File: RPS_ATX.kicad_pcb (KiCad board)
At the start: 2 copper layers, 100 x 50 mm, 89 parts, among them J1 5V, J2 C1, J3 C2, J4 17.5V, J5 PS_OUT-, J6 PS_OUT+, J7 RPS_OUT+, J8 Conn_01x05, J9 RPS_OUT-, Q1 AO3400A, Q3 BSS138, SW1 RST, U1 TL494, U2 AMS1117-3.3, U3 L7815, U4 NE5532, U5 INA180A2, U6 ICL7660, U7 LM7805_TO220, U8 STM32G431RBT6, Y1 8MHz

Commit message: approximate location of the components at the PCB
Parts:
- removed SW1: RST, Button_Switch_SMD:SW_Push_1P1T_NO_E-Switch_TL3301NxxxxxG
- added SW2: RST, Button_Switch_SMD:SW_Push_1P1T_NO_E-Switch_TL3301NxxxxxG, F.Cu at (132.3, 93.8)
- J8: value Conn_01x05 -> SWD
- moved Q1 209.6 mm to (66.9, 93.0), turned to 180 degrees
- moved C17 201.9 mm to (79.5, 97.0), turned to 180 degrees
- moved C13 200.8 mm to (84.5, 99.6)
- moved C14 192.2 mm to (90.5, 94.9), turned to -90 degrees
- moved FB2 190.0 mm to (104.9, 87.9), turned to -90 degrees
- moved J3 186.9 mm to (88.1, 57.5)
- moved R12 185.6 mm to (61.8, 93.0), turned to 180 degrees
- moved J2 184.8 mm to (91.9, 57.5)
- moved TP1 184.6 mm to (91.2, 99.2), turned to 90 degrees
- moved C3 176.0 mm to (82.6, 71.3), turned to 180 degrees
- moved R10 175.9 mm to (105.0, 82.7), turned to 90 degrees
- moved C19 175.0 mm to (83.6, 65.8), turned to 90 degrees
- moved R19 174.5 mm to (119.4, 71.6), turned to 90 degrees
- moved C28 174.1 mm to (107.4, 87.8), turned to -90 degrees
- moved C30 171.9 mm to (107.4, 82.7), turned to 90 degrees
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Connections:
- net MEAS_U+ renamed VOUT
- C1 pad 2: MEAS_I- -> GND
- C10 pad 2: MEAS_I- -> GND
- C11 pad 2: MEAS_I- -> GND
- C12 pad 2: MEAS_I- -> GND
- C13 pad 2: MEAS_I- -> GND
- C14 pad 2: MEAS_I- -> GND
- C16 pad 2: MEAS_I- -> GND
- C17 pad 1: +17.5V_ATX -> GND
- C17 pad 2: MEAS_I- -> +5V
- C18 pad 2: MEAS_I- -> GND
- C19 pad 2: MEAS_I- -> GND
- C2 pad 2: MEAS_I- -> GND
- C21 pad 2: MEAS_I- -> GND
- C22 pad 2: MEAS_I- -> GND
- C23 pad 2: MEAS_I- -> GND
- C24 pad 2: MEAS_I- -> GND
- C25 pad 2: MEAS_I- -> GND
- C26 pad 2: MEAS_I- -> GND
- C27 pad 2: MEAS_I- -> GND
- C28 pad 2: MEAS_I- -> GND
- C29 pad 2: MEAS_I- -> GND
- C3 pad 2: MEAS_I- -> GND
- C30 pad 2: MEAS_I- -> GND
- C31 pad 2: MEAS_I- -> GND
- C32 pad 2: MEAS_I- -> GND
- C33 pad 2: MEAS_I- -> GND
- C4 pad 1: MEAS_I- -> GND
- C5 pad 2: MEAS_I- -> GND
- C6 pad 2: MEAS_I- -> GND
- C7 pad 2: MEAS_I- -> GND
- C8 pad 2: MEAS_I- -> GND
- C9 pad 2: MEAS_I- -> GND
- J5 pad 1: MEAS_I- -> GND
- J8 pad 1: MCU_SWDIO -> MCU_RST
- J8 pad 2: MCU_SWCLK -> MCU_SWDIO
- J8 pad 3: MCU_SWO -> MCU_SWCLK
- J8 pad 4: MCU_RST -> MCU_SWO
- J8 pad 5: MEAS_I- -> GND
- Q3 pad 2: MEAS_I- -> GND
- R11 pad 1: MEAS_I- -> GND
- R18 pad 1: MEAS_I- -> GND
- R23 pad 2: MEAS_I- -> GND
- R3 pad 1: MEAS_I- -> GND
- R8 pad 2: MEAS_I- -> GND
- R9 pad 2: MEAS_I- -> GND
- U1 pad 10: MEAS_I- -> GND
- U1 pad 7: MEAS_I- -> GND
- U1 pad 9: MEAS_I- -> GND
- U2 pad 1: MEAS_I- -> GND
- U3 pad 2: MEAS_I- -> GND
- U4 pad 5: MEAS_I- -> GND
- U5 pad 2: MEAS_I- -> GND
- U6 pad 3: MEAS_I- -> GND
- U7 pad 2: MEAS_I- -> GND
- U8 pad 15: MEAS_I- -> GND
- U8 pad 27: MEAS_I- -> GND
- U8 pad 31: MEAS_I- -> GND
- U8 pad 47: MEAS_I- -> GND
- U8 pad 63: MEAS_I- -> GND

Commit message: final location of the power,analog sections
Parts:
- removed SW2: RST, Button_Switch_SMD:SW_Push_1P1T_NO_E-Switch_TL3301NxxxxxG
- added JP1: RST, TestPoint:TestPoint_2Pads_Pitch2.54mm_Drill0.8mm, F.Cu at (127.0, 100.3)
- added L1: L, my lib:Resistor_Shunt_L10_D3.7, F.Cu at (59.8, 63.2)
- added R20: 5.1K, Resistor_SMD:R_1206_3216Metric_Pad1.30x1.75mm_HandSolder, F.Cu at (121.0, 100.3)
- Y1: footprint Crystal:Crystal_SMD_MicroCrystal_CC1V-T1A-2Pin_8.0x3.7mm_HandSoldering -> Crystal:Crystal_SMD_0603-2Pin_6.0x3.5mm_HandSoldering
- moved C10 63.4 mm to (172.1, 122.6)
- moved C6 63.4 mm to (172.1, 115.1)
- moved J1 63.4 mm to (184.2, 111.5)
- moved J4 63.4 mm to (178.8, 113.1)
- moved TP2 63.4 mm to (173.8, 128.0)
- moved U3 63.4 mm to (183.7, 118.6)
- moved U7 63.4 mm to (181.2, 125.0)
- moved C12 63.4 mm to (178.5, 128.6)
- moved TP3 63.4 mm to (178.0, 132.8)
- moved C11 45.5 mm to (188.3, 95.6)
- moved C1 45.5 mm to (185.8, 97.8)
- moved TP4 45.5 mm to (195.2, 88.7)
- moved U2 45.5 mm to (194.2, 96.8)
- moved TP1 26.5 mm to (108.2, 119.5)
- moved C15 23.9 mm to (121.4, 116.7)
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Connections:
- C18 pad 1: U_1IN- -> U_1IN+
- C9 pad 1: I_2IN- -> I_2IN+
- J6 pad 1: VOUT -> Net-(J6-Pin_1)
- R14 pad 2: U_1IN- -> U_1IN+
- R24 pad 2: Net-(U1-1IN+) -> U_1IN-
- R25 pad 2: Net-(U1-2IN+) -> I_2IN-
- R5 pad 2: I_2IN- -> I_2IN+
- U1 pad 1: Net-(U1-1IN+) -> U_1IN+
- U1 pad 16: Net-(U1-2IN+) -> I_2IN+
- U8 pad 12: MCU_ADC_U -> unconnected-(U8-PA0-Pad12)
- U8 pad 13: MCU_ADC_I -> MCU_494_ON
- U8 pad 20: unconnected-(U8-PA6-Pad20) -> MCU_ADC_I
- U8 pad 21: unconnected-(U8-PA7-Pad21) -> MCU_ADC_U
- U8 pad 24: MCU_DCH -> unconnected-(U8-PB0-Pad24)
- U8 pad 33: unconnected-(U8-PB11-Pad33) -> MCU_DCH
- U8 pad 45: MCU_494_ON -> unconnected-(U8-PA11-Pad45)

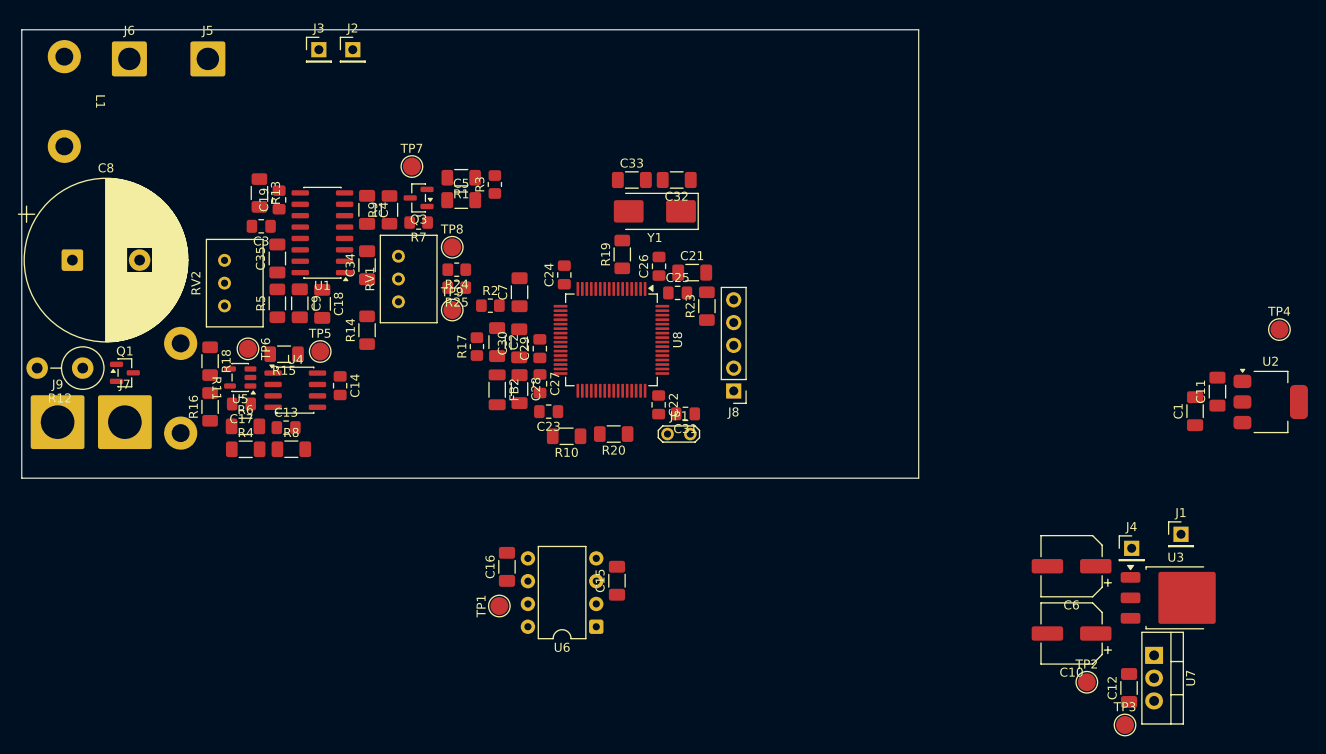
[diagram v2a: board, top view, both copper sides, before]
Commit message: power/analog lines are finished
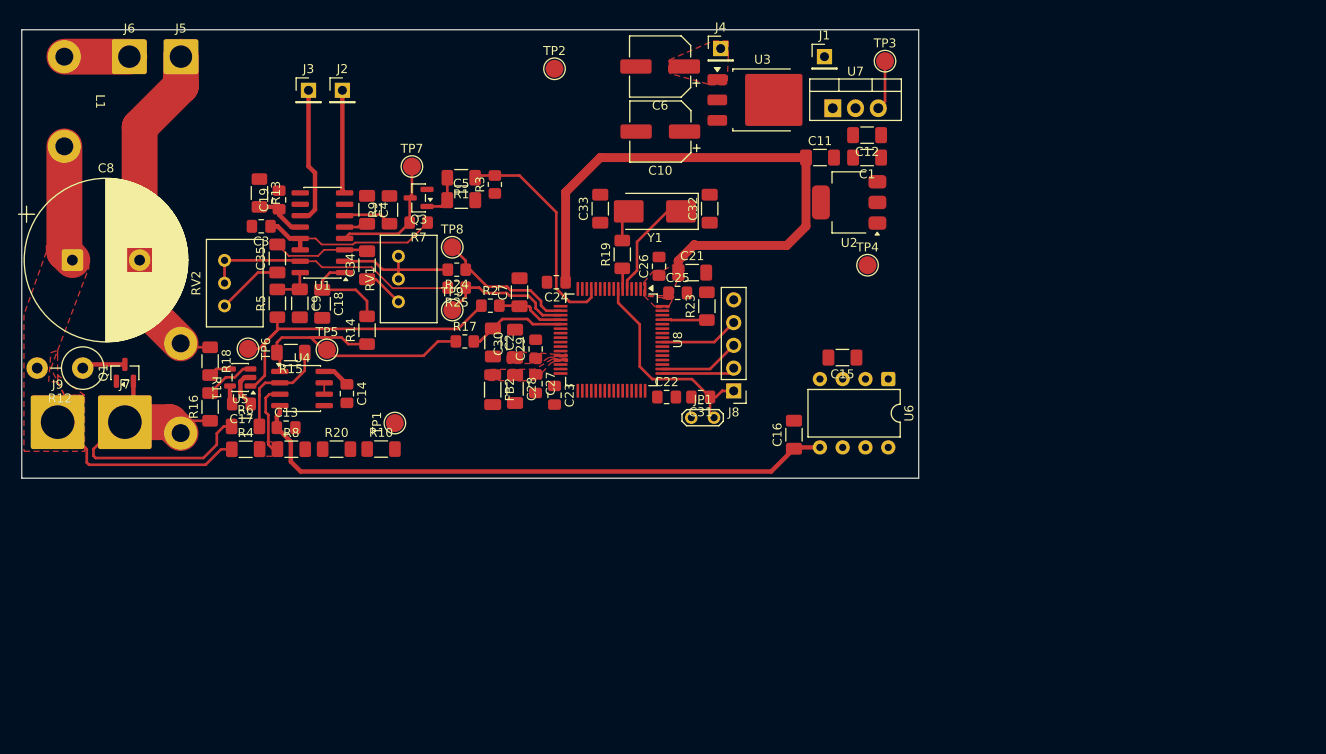
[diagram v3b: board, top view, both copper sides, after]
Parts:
- moved TP2 90.6 mm to (114.4, 59.6)
- moved TP3 78.7 mm to (151.2, 58.8)
- moved C10 72.3 mm to (126.2, 66.6)
- moved C6 72.2 mm to (126.2, 59.3)
- moved U3 72.1 mm to (137.6, 63.1)
- moved J4 72.1 mm to (132.9, 57.3)
- moved U7 70.7 mm to (145.4, 64.0), turned to 0 degrees
- moved C12 68.2 mm to (149.2, 67.0), turned to 180 degrees
- moved J1 66.5 mm to (144.5, 58.2)
- moved U2 52.0 mm to (147.2, 74.5), turned to 180 degrees
- moved C11 51.4 mm to (144.0, 69.5), turned to 0 degrees
- moved TP4 46.5 mm to (149.3, 81.5)
- moved C1 46.2 mm to (149.2, 69.5), turned to 180 degrees
- moved U6 42.7 mm to (151.6, 94.2), turned to -90 degrees
- moved C15 35.4 mm to (146.5, 91.8), turned to 180 degrees
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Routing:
- net -5V: track 0.00 -> 67.8 mm
- net +3.3V: track 0.00 -> 63.3 mm
- net GND: track 0.09 -> 43.6 mm
- net MEAS_I+: track 0.00 -> 39.2 mm
- net /Analog/i_op_out: track 0.00 -> 37.4 mm
- net VOUT: track 0.00 -> 36.0 mm
- net Net-(R14-Pad1): track 0.00 -> 34.2 mm
- net I_2IN-: track 0.00 -> 28.7 mm
- net MCU_RST: track 0.00 -> 25.3 mm
- net MCU_494_ON: track 0.00 -> 25.0 mm
- net +5V_REF: track 0.00 -> 20.6 mm
- net MCU_DAC_U: track 0.00 -> 15.9 mm
- net C2: track 0.00 -> 15.5 mm
- net MCU_DAC_I: track 0.00 -> 15.3 mm
- net U_1IN-: track 0.00 -> 14.4 mm
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- added copper zone on F.Cu, net +17.5V_ATX
- added copper zone on F.Cu, net +3.3V
- added copper zone on F.Cu, net /Digital/mcu_vref
- added copper zone on F.Cu, net Net-(U4A-+)
- added copper zone on F.Cu, net Net-(U8-VDDA)
- added copper zone on F.Cu, net VOUT

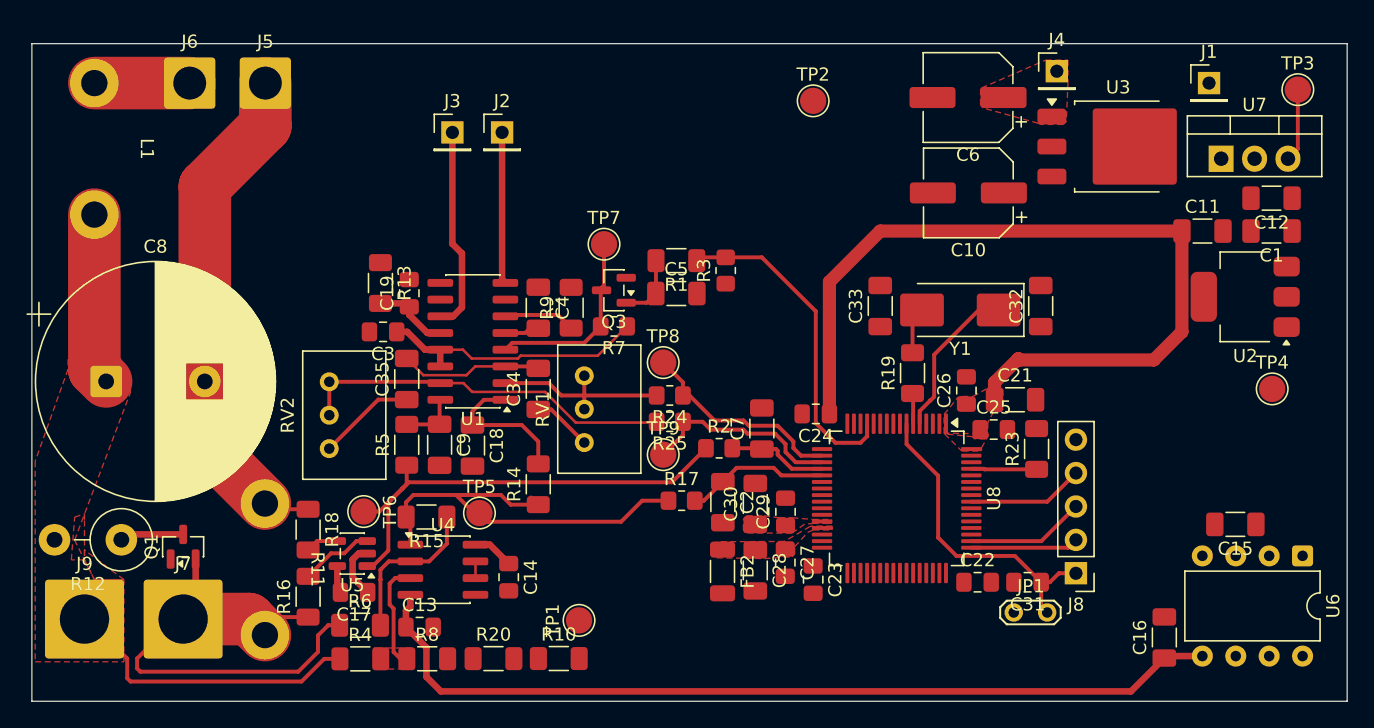
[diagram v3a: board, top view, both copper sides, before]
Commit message: added display and encoders signal lines, hints
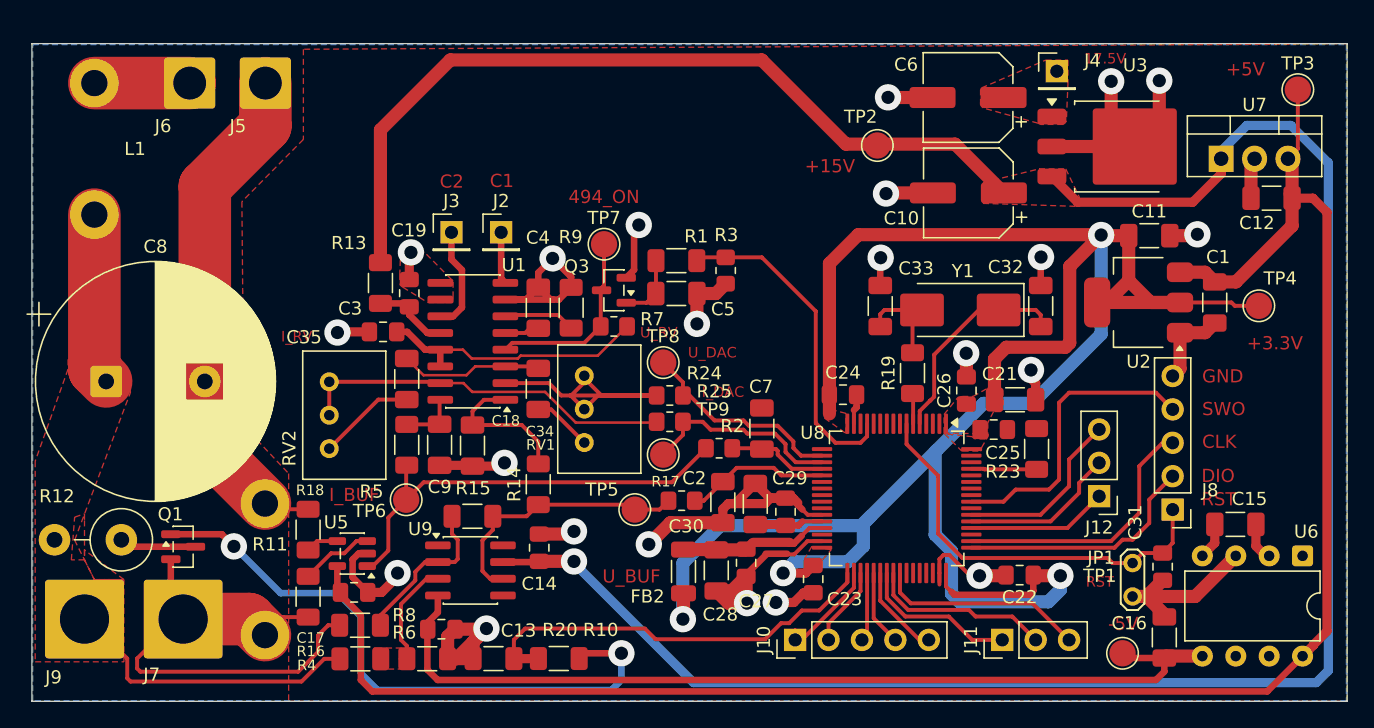
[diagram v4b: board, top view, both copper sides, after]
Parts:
- removed J1: 5V, Connector_PinHeader_2.54mm:PinHeader_1x01_P2.54mm_Vertical
- removed U4: NE5532, Package_SO:SOIC-8_3.9x4.9mm_P1.27mm
- added J10: DISP, Connector_PinHeader_2.54mm:PinHeader_1x05_P2.54mm_Vertical, F.Cu at (113.0, 100.6)
- added J11: ENC1, Connector_PinHeader_2.54mm:PinHeader_1x03_P2.54mm_Vertical, F.Cu at (128.8, 100.6)
- added J12: ENC2, Connector_PinHeader_2.54mm:PinHeader_1x03_P2.54mm_Vertical, F.Cu at (136.1, 89.7)
- added U9: OP07, Package_SO:SOIC-8_3.9x4.9mm_P1.27mm, F.Cu at (88.3, 95.3)
- RV1: value 100K -> U_RV
- RV2: value 100K -> I_RV
- moved TP1 41.4 mm to (137.9, 101.6)
- moved TP5 11.8 mm to (100.8, 90.7)
- moved C31 10.3 mm to (141.0, 95.0), turned to -90 degrees
- moved JP1 9.12 mm to (138.7, 97.3), turned to 90 degrees
- moved J8 8.80 mm to (141.7, 90.7)
- moved U2 8.12 mm to (139.1, 74.9)
- moved J2 7.60 mm to (90.7, 69.6)
- moved J3 7.60 mm to (86.9, 69.6)
- moved C1 6.94 mm to (144.9, 74.9), turned to -90 degrees
- moved TP4 6.40 mm to (148.3, 75.2)
- moved TP2 5.94 mm to (119.3, 63.0)
- moved C11 4.06 mm to (140.0, 69.8)
- moved R15 3.49 mm to (88.5, 91.2), turned to 0 degrees
- moved TP6 3.35 mm to (83.5, 89.9)
- moved C22 3.24 mm to (130.1, 95.7), turned to 180 degrees
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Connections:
- U8 pad 34: unconnected-(U8-PB12-Pad34) -> DISP_DC
- U8 pad 35: unconnected-(U8-PB13-Pad35) -> DISP_SCK
- U8 pad 36: unconnected-(U8-PB14-Pad36) -> DISP_RST
- U8 pad 37: unconnected-(U8-PB15-Pad37) -> DISP_MOSI
- U8 pad 38: unconnected-(U8-PC6-Pad38) -> DISP_CS
- U8 pad 39: unconnected-(U8-PC7-Pad39) -> ENC1_KEY
- U8 pad 40: unconnected-(U8-PC8-Pad40) -> ENC1_S1
- U8 pad 41: unconnected-(U8-PC9-Pad41) -> ENC1_S2
- U8 pad 52: unconnected-(U8-PC10-Pad52) -> ENC2_KEY
- U8 pad 53: unconnected-(U8-PC11-Pad53) -> ENC2_S1
- U8 pad 54: unconnected-(U8-PC12-Pad54) -> ENC2_S2
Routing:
- net +15V: track 3.50 -> 196.0 mm, vias 0 -> 1
- net GND: track 43.6 -> 205.2 mm, vias 0 -> 22
- net +5V: track 7.67 -> 141.9 mm
- net +3.3V: track 63.3 -> 175.4 mm, vias 0 -> 4
- net Net-(Q1-G): track 0.00 -> 47.4 mm, vias 0 -> 2
- net MCU_DCH: track 0.00 -> 31.8 mm
- net ENC1_S2: track 0.00 -> 15.8 mm
- net ENC1_S1: track 0.00 -> 13.9 mm
- net MCU_SWO: track 8.85 -> 22.7 mm
- net Net-(R14-Pad1): track 34.2 -> 20.5 mm
- net ENC2_S2: track 0.00 -> 13.6 mm
- net U_1IN-: track 14.4 -> 27.5 mm
- net ENC2_S1: track 0.00 -> 12.0 mm
- net ENC1_KEY: track 0.00 -> 12.0 mm
- net MCU_SWCLK: track 9.05 -> 20.5 mm
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- added copper zone on F.Cu, net +15V
- added copper zone on B.Cu, net GND
- added copper zone on F.Cu, net GND
- removed copper zone on F.Cu, net /Digital/mcu_vref
- removed copper zone on F.Cu, net Net-(U8-VDDA)
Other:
- board text added: "CLK"
- board text added: "DIO"
- board text added: "GND"
- board text added: "RST"
- board text added: "SWO"
